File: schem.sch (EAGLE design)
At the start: 25 parts

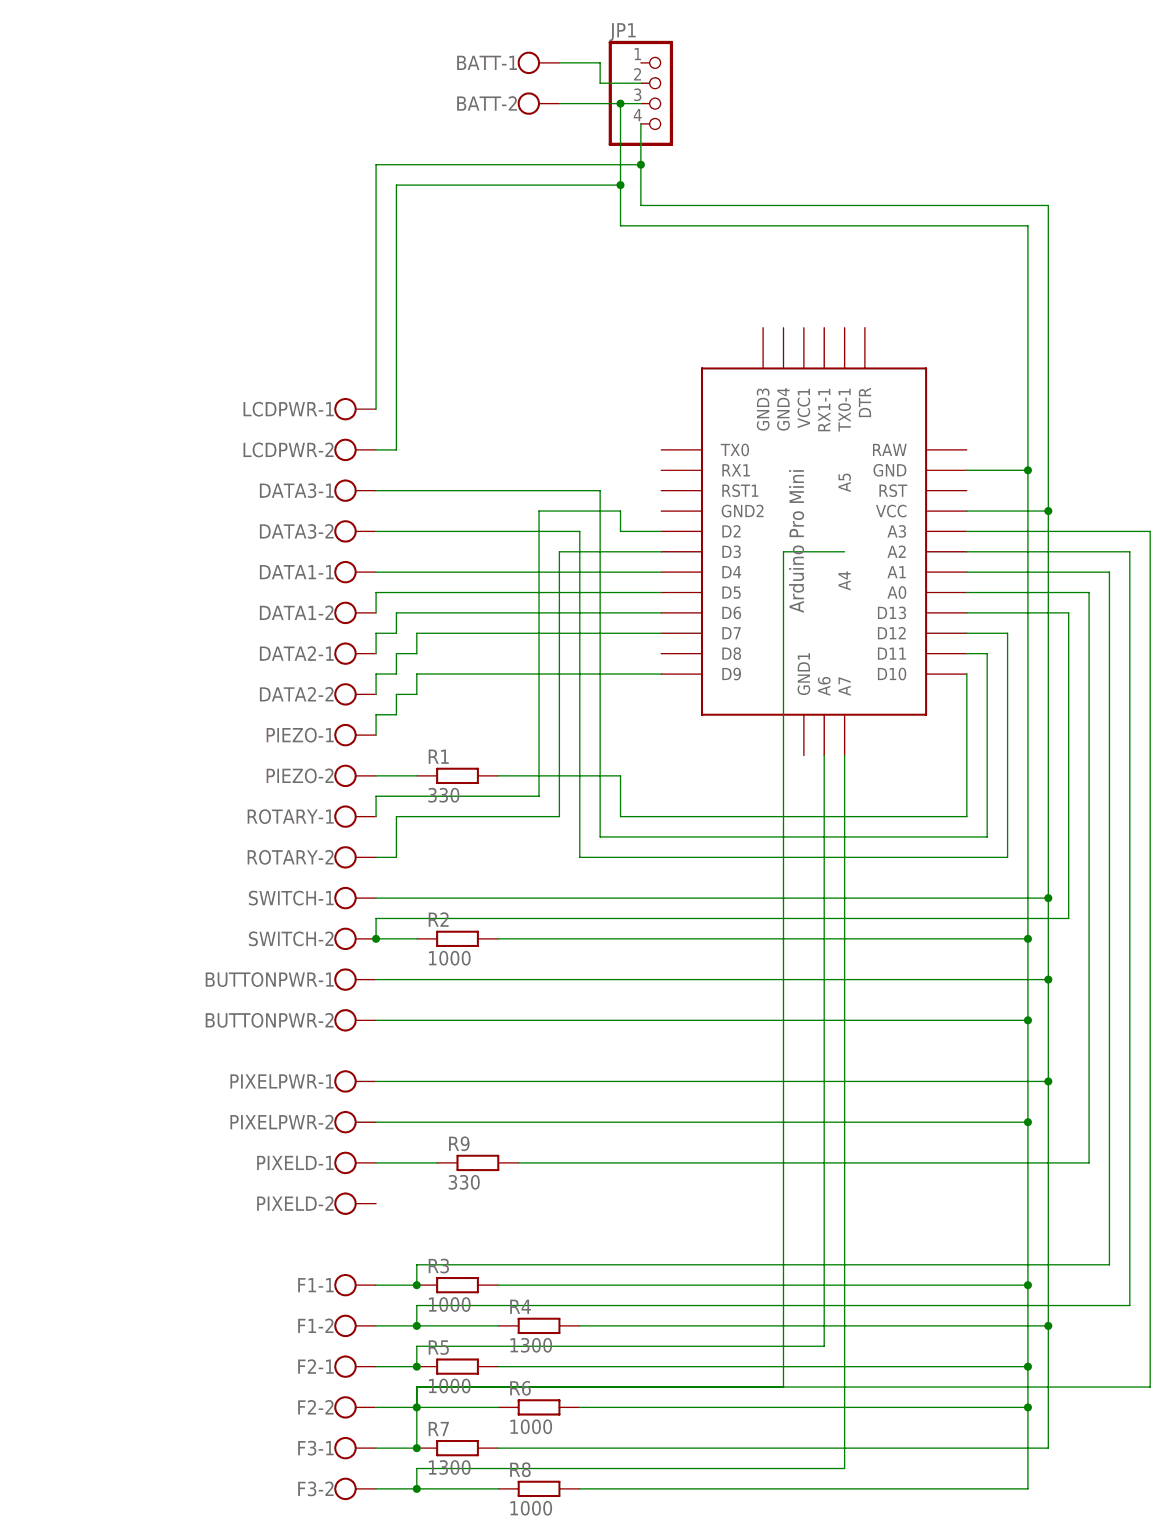
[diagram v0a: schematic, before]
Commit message: New Molex version of PCB
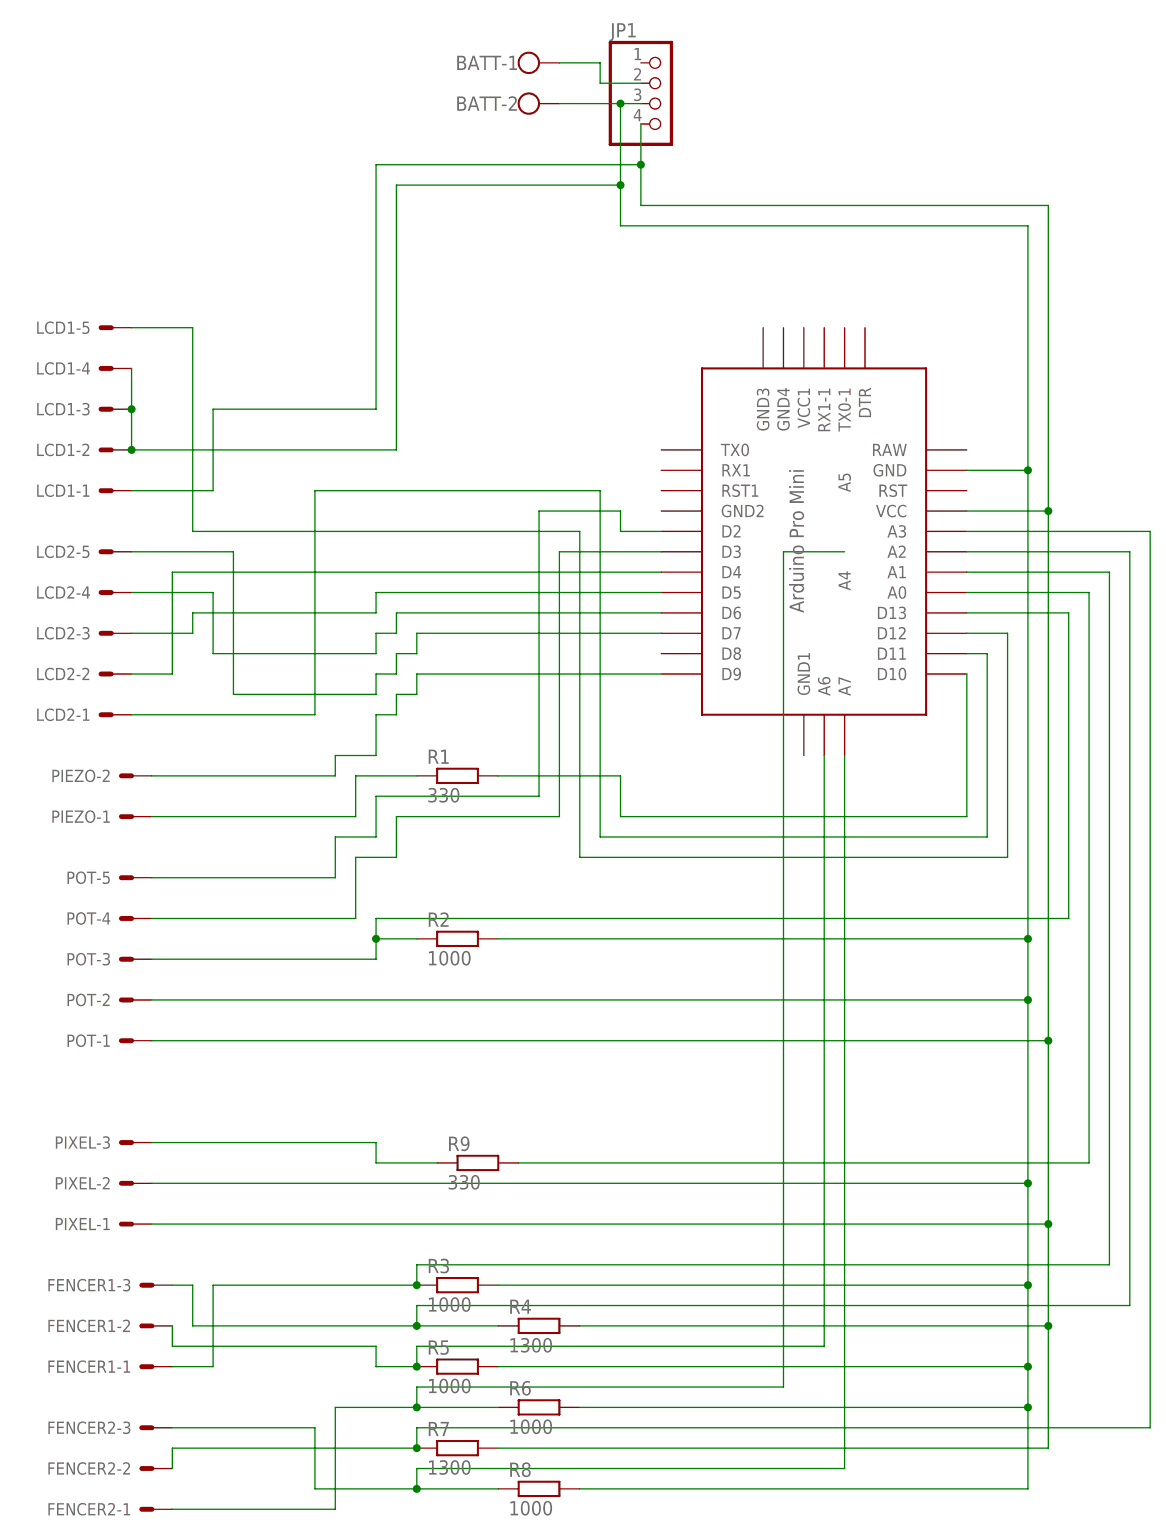
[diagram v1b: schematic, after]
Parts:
- removed BUTTONPWR, DATA1, DATA2, DATA3, F1, F2, F3, LCDPWR, PIXELD, PIXELPWR, ROTARY, SWITCH: (no value), con-wago-500:W237-102
- added FENCER1, FENCER2, PIXEL: 22-27-2031-03, EP_molex_6410_7395:22-27-2031-03
- added LCD1, LCD2, POT: 22-27-2051-05, EP_molex_6410_7395:22-27-2051-05
- PIEZO: value (none) -> 22-27-2021-02; device con-wago-500:W237-102 -> EP_molex_6410_7395:22-27-2021-02
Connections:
- new net N$24: FENCER2-2.S, R7.1, U$1.A3
- net N$1: now also LCD1-1.S, PIXEL-1.S, POT-1.S; no longer BUTTONPWR-1.KL, LCDPWR-1.KL, PIXELPWR-1.KL, SWITCH-1.KL
- net N$10: now also PIEZO-2.S; no longer PIEZO-1.KL
- net N$11: now also PIEZO-1.S; no longer PIEZO-2.KL
- net N$13: now also POT-5.S; no longer ROTARY-1.KL
- net N$14: now also POT-4.S; no longer ROTARY-2.KL
- net N$15: now also FENCER1-1.S; no longer F1-1.KL
- net N$16: now also POT-3.S; no longer SWITCH-2.KL
- net N$18: now also FENCER1-3.S; no longer F1-2.KL
- net N$19: now also FENCER1-2.S; no longer F2-1.KL
- net N$2: now also LCD1-2.S, LCD1-3.S, LCD1-4.S, PIXEL-2.S, POT-2.S; no longer BUTTONPWR-2.KL, LCDPWR-2.KL, PIXELPWR-2.KL
- net N$20: now also FENCER2-1.S; no longer F2-2.KL, F3-1.KL, R7.1, U$1.A3
- net N$22: now also FENCER2-3.S; no longer F3-2.KL
- net N$23: now also PIXEL-3.S; no longer PIXELD-1.KL
- net N$4: now also LCD2-4.S; no longer DATA2-1.KL
- net N$5: now also LCD2-1.S; no longer DATA3-1.KL
- net N$6: now also LCD1-5.S; no longer DATA3-2.KL
- net N$7: now also LCD2-2.S; no longer DATA1-1.KL
- net N$8: now also LCD2-3.S; no longer DATA1-2.KL
- net N$9: now also LCD2-5.S; no longer DATA2-2.KL
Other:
- moved on the sheet: PIEZO-1, PIEZO-2
